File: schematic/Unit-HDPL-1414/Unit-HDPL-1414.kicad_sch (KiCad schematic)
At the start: 5 parts, among them J1 Conn_01x04

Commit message: schematic src
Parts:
- removed H1: MountingHole, symbol Mechanical:MountingHole
- added H1: M5Unit_Screw_Hole, footprints:unit_mounting_hole, symbol Unit-HDPL:unit_mouting_hole
- J1: footprint (none) -> footprints:HY2.0-4P
- U1: value ~ -> M5StampS3; footprint (none) -> footprints:M5StampS3
- U2, U3: value ~ -> HPDL-1414; footprint (none) -> footprints:HPDL-1414
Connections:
- net +5V: now also U1.13 (5V); no longer U1. (GND)
- net GND: now also U1.18 (GND); no longer U1. (GND)
- net at J1.3 (Pin_3): now also U1.15 (G13/SDA); no longer U1. (GND)
- net at J1.4 (Pin_4): now also U1.17 (G15/SCL); no longer U1. (GND)
- net at U2.1 (D6), U3.1 (D6): now also U1.27 (G46); no longer U1. (GND)
- net at U2.10 (D2), U3.10 (D2): now also U1.5 (G5); no longer U1. (GND)
- net at U2.11 (D3), U3.11 (D3): now also U1.7 (G7); no longer U1. (GND)
- net at U2.12 (D5), U3.12 (D5): now also U1.9 (G9); no longer U1. (GND)
- net at U2.2 (D4), U3.2 (D4): now also U1.26 (G43); no longer U1. (GND)
- net at U3.3 (WR): now also U1.25 (G42); no longer U1. (GND)
- net at U2.4 (A1), U3.4 (A1): now also U1.23 (G41); no longer U1. (GND)
- net at U2.5 (A0), U3.5 (A0): now also U1.21 (G40); no longer U1. (GND)
- net at U2.8 (D0), U3.8 (D0): now also U1.1 (G1); no longer U1. (GND)
- net at U2.9 (D1), U3.9 (D1): now also U1.3 (G3); no longer U1. (GND)
- net at U2.3 (WR): now also U1.24 (G44); no longer U1. (GND)

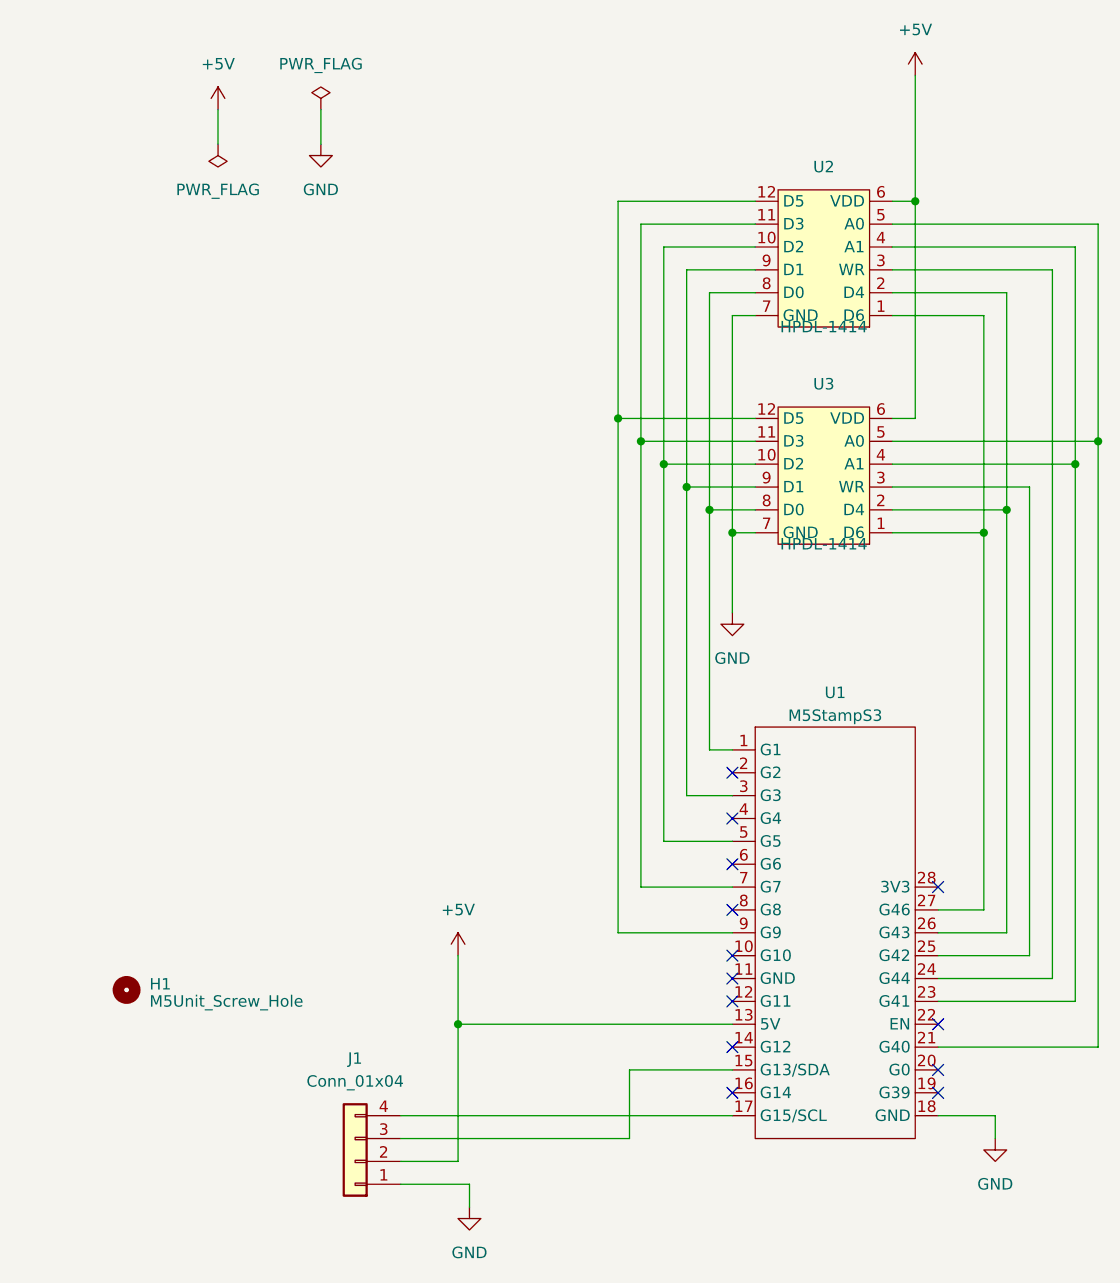
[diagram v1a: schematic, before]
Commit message: 基板ピン配置ミス修正
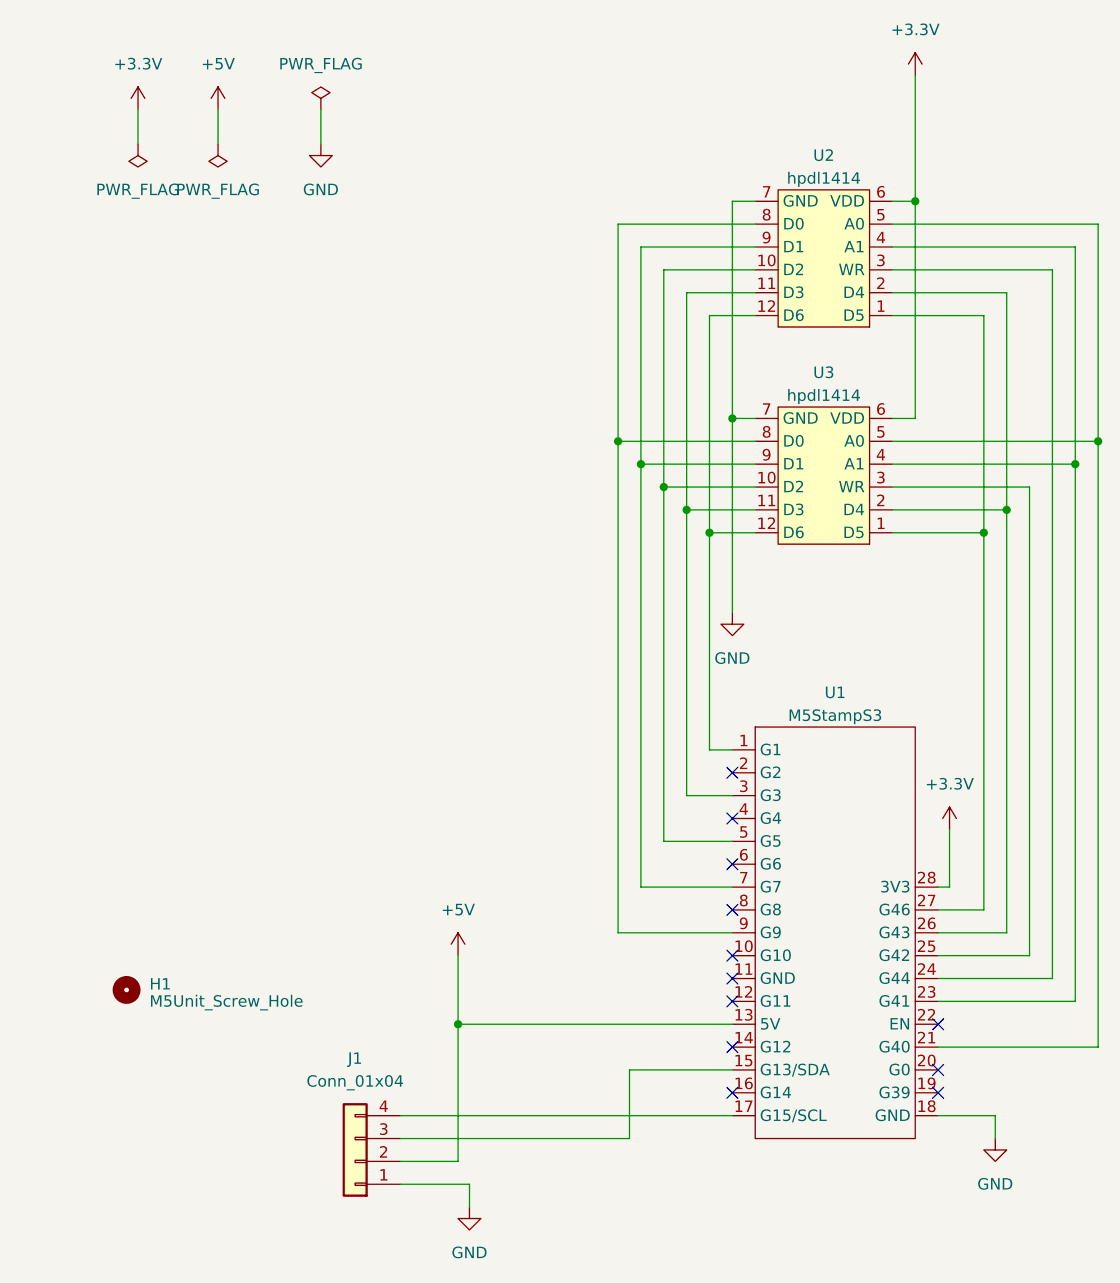
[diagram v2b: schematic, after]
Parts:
- U2, U3: value HPDL-1414 -> hpdl1414
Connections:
- net +5V: no longer U2.6 (VDD), U3.6 (VDD)
- net at U2.8 (D0), U3.8 (D0): now also U1.9 (G9); no longer U1.1 (G1)
- net +3.3V: now reaches U1.28 (3V3)
- net +3.3V: now also U2.6 (VDD), U3.6 (VDD)
- net at U2.9 (D1), U3.9 (D1): now also U1.7 (G7); no longer U1.3 (G3)
- net at U2.11 (D3), U3.11 (D3): now also U1.3 (G3); no longer U1.7 (G7)
- net at U2.12 (D6), U3.12 (D6): now also U1.1 (G1); no longer U1.9 (G9)
- no-connect marks 13 -> 12
